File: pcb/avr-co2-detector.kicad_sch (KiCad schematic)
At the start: 7 parts

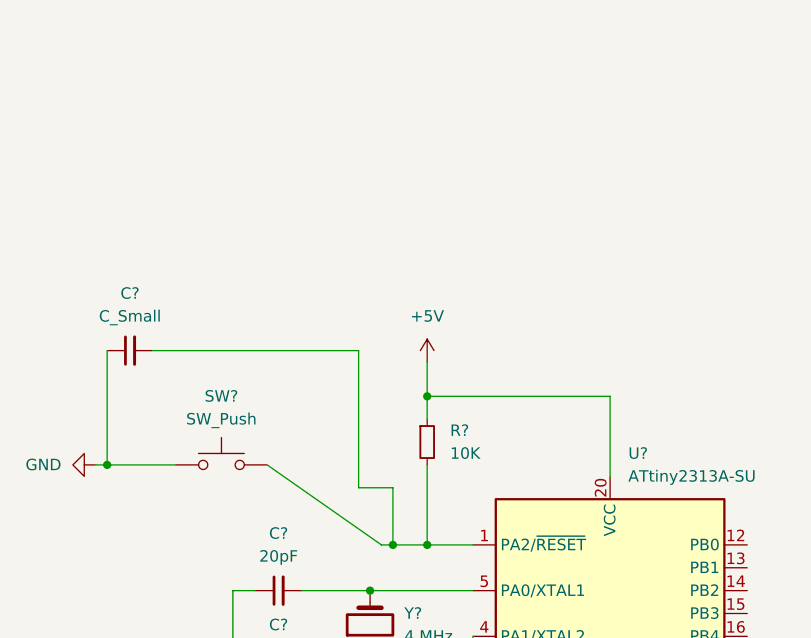
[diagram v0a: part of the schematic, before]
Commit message: Added USB Type-C connector for power supply, decoupling capacitor for ATtiny2313A
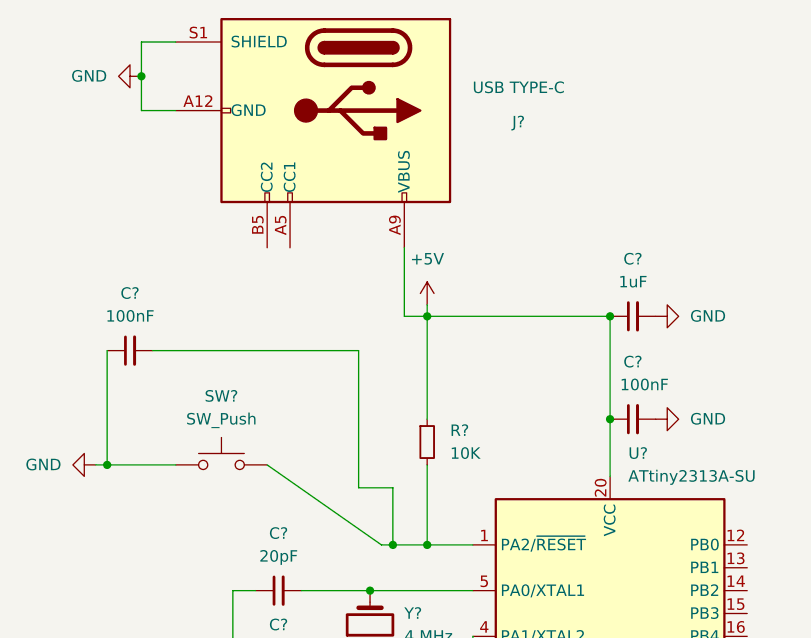
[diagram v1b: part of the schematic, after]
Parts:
- added C?: 1uF, symbol Device:C_Small
- added C?: 100nF, symbol Device:C_Small
- added J?: USB TYPE-C, Connector_USB:USB_C_Receptacle_HRO_TYPE-C-31-M-12, symbol Connector:USB_C_Receptacle_PowerOnly_6P
- C?: value C_Small -> 100nF
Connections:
- net +5V: now also C?.1, C?.1, J?.A9 (VBUS), J?.B9 (VBUS)
- net GND: now also C?.2, C?.2, J?.A12 (GND), J?.B12 (GND), J?.S1 (SHIELD)
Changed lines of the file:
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@@
 (kicad_sch (version 20211123) (generator eeschema)
   (paper "A4")
+  (junction (at 78.74 46.99) (diameter 0) (color 0 0 0 0)
+  )
   (junction (at 88.9 114.3) (diameter 0) (color 0 0 0 0)
   )
@@
   (junction (at 104.14 111.76) (diameter 0) (color 0 0 0 0)
   )
+  (junction (at 130.81 85.09) (diameter 0) (color 0 0 0 0)
+  )
+  (junction (at 110.49 73.66) (diameter 0) (color 0 0 0 0)
+  )
   (junction (at 106.68 99.06) (diameter 0) (color 0 0 0 0)
   )
-  (junction (at 110.49 82.55) (diameter 0) (color 0 0 0 0)
-  )
   (junction (at 110.49 99.06) (diameter 0) (color 0 0 0 0)
   )
   (junction (at 104.14 104.14) (diameter 0) (color 0 0 0 0)
   )
-  (wire (pts (xy 130.81 91.44) (xy 130.81 82.55))
+  (junction (at 130.81 73.66) (diameter 0) (color 0 0 0 0)
+  )
+  (wire (pts (xy 78.74 43.18) (xy 78.74 46.99))
+    (stroke (width 0) (type default) (color 0 0 0 0))
+  )
+  (wire (pts (xy 107.95 66.04) (xy 107.95 73.66))
     (stroke (width 0) (type default) (color 0 0 0 0))
   )
@@
     (stroke (width 0) (type default) (color 0 0 0 0))
   )
+  (wire (pts (xy 82.55 43.18) (xy 78.74 43.18))
+    (stroke (width 0) (type default) (color 0 0 0 0))
+  )
   (wire (pts (xy 104.14 104.14) (xy 115.57 104.14))
     (stroke (width 0) (type default) (color 0 0 0 0))
@@
     (stroke (width 0) (type default) (color 0 0 0 0))
   )
+  (wire (pts (xy 110.49 73.66) (xy 130.81 73.66))
+    (stroke (width 0) (type default) (color 0 0 0 0))
+  )
   (wire (pts (xy 105.41 99.06) (xy 106.68 99.06))
     (stroke (width 0) (type default) (color 0 0 0 0))
   )
+  (wire (pts (xy 82.55 50.8) (xy 78.74 50.8))
+    (stroke (width 0) (type default) (color 0 0 0 0))
+  )
   (wire (pts (xy 88.9 104.14) (xy 88.9 114.3))
     (stroke (width 0) (type default) (color 0 0 0 0))
@@
     (stroke (width 0) (type default) (color 0 0 0 0))
   )
-  (wire (pts (xy 110.49 82.55) (xy 110.49 85.09))
+  (wire (pts (xy 130.81 73.66) (xy 130.81 85.09))
+    (stroke (width 0) (type default) (color 0 0 0 0))
+  )
+  (wire (pts (xy 110.49 73.66) (xy 110.49 85.09))
     (stroke (width 0) (type default) (color 0 0 0 0))
   )
@@
     (stroke (width 0) (type default) (color 0 0 0 0))
   )
+  (wire (pts (xy 130.81 85.09) (xy 130.81 91.44))
+    (stroke (width 0) (type default) (color 0 0 0 0))
+  )
   (wire (pts (xy 115.57 111.76) (xy 115.57 109.22))
     (stroke (width 0) (type default) (color 0 0 0 0))
@@
     (stroke (width 0) (type default) (color 0 0 0 0))
   )
-  (wire (pts (xy 110.49 82.55) (xy 130.81 82.55))
+  (wire (pts (xy 107.95 73.66) (xy 110.49 73.66))
     (stroke (width 0) (type default) (color 0 0 0 0))
   )
@@
     (stroke (width 0) (type default) (color 0 0 0 0))
   )
-  (wire (pts (xy 110.49 78.74) (xy 110.49 82.55))
+  (wire (pts (xy 110.49 72.39) (xy 110.49 73.66))
     (stroke (width 0) (type default) (color 0 0 0 0))
   )
   (wire (pts (xy 102.87 77.47) (xy 102.87 92.71))
+    (stroke (width 0) (type default) (color 0 0 0 0))
+  )
+  (wire (pts (xy 78.74 50.8) (xy 78.74 46.99))
     (stroke (width 0) (type default) (color 0 0 0 0))
   )
@@
     (pin "1")
   )
+  (symbol (lib_id "Device:C_Small") (at 133.35 73.66 90) (unit 1)
+    (in_bom yes) (on_board yes)
+    (property "Reference" "C?" (id 0) (at 133.3563 67.31 90))
+    (property "Value" "1uF" (id 1) (at 133.3563 69.85 90))
+    (property "Footprint" "" (id 2) (at 133.35 73.66 0)
+      (effects (font (size 1.27 1.27)) hide)
+    )
+    (property "Datasheet" "~" (id 3) (at 133.35 73.66 0)
+      (effects (font (size 1.27 1.27)) hide)
+    )
+    (pin "1")
+    (pin "2")
+  )
+  (symbol (lib_id "power:GND") (at 135.89 85.09 90) (unit 1)
+    (in_bom yes) (on_board yes) (fields_autoplaced)
+    (property "Reference" "#PWR?" (id 0) (at 142.24 85.09 0)
+      (effects (font (size 1.27 1.27)) hide)
+    )
+    (property "Value" "GND" (id 1) (at 139.7 85.0899 90)
+      (effects (font (size 1.27 1.27)) (justify right))
+    )
+    (property "Footprint" "" (id 2) (at 135.89 85.09 0)
+      (effects (font (size 1.27 1.27)) hide)
+    )
+    (property "Datasheet" "" (id 3) (at 135.89 85.09 0)
+      (effects (font (size 1.27 1.27)) hide)
+    )
+    (pin "1")
+  )
   (symbol (lib_id "Device:R_Small") (at 110.49 87.63 0) (unit 1)
     (in_bom yes) (on_board yes) (fields_autoplaced)
@@
     (pin "1")
     (pin "2")
+  )
+  (symbol (lib_id "power:GND") (at 78.74 46.99 270) (unit 1)
+    (in_bom yes) (on_board yes) (fields_autoplaced)
+    (property "Reference" "#PWR?" (id 0) (at 72.39 46.99 0)
+      (effects (font (size 1.27 1.27)) hide)
+    )
+    (property "Value" "GND" (id 1) (at 74.93 46.9899 90)
+      (effects (font (size 1.27 1.27)) (justify right))
+    )
+    (property "Footprint" "" (id 2) (at 78.74 46.99 0)
+      (effects (font (size 1.27 1.27)) hide)
+    )
+    (property "Datasheet" "" (id 3) (at 78.74 46.99 0)
+      (effects (font (size 1.27 1.27)) hide)
+    )
+    (pin "1")
   )
   (symbol (lib_id "MCU_Microchip_ATtiny:ATtiny2313A-S") (at 130.81 119.38 0) (unit 1)
@@
     (pin "2")
   )
+  (symbol (lib_id "Connector:USB_C_Receptacle_PowerOnly_6P") (at 100.33 50.8 270) (unit 1)
+    (in_bom yes) (on_board yes)
+    (property "Reference" "J?" (id 0) (at 120.65 52.07 90))
+    (property "Value" "USB TYPE-C" (id 1) (at 120.65 48.26 90))
+    (property "Footprint" "Connector_USB:USB_C_Receptacle_HRO_TYPE-C-31-M-12" (id 2) (at 102.87 54.61 0)
+      (effects (font (size 1.27 1.27)) hide)
+    )
+    (property "Datasheet" "https://www.usb.org/sites/default/files/documents/usb_type-c.zip" (id 3) (at 100.33 50.8 0)
+      (effects (font (size 1.27 1.27)) hide)
+    )
+    (pin "A12")
+    (pin "A5")
+    (pin "A9")
+    (pin "B12")
+    (pin "B5")
+    (pin "B9")
+    (pin "S1")
+  )
   (symbol (lib_id "power:GND") (at 73.66 90.17 270) (unit 1)
     (in_bom yes) (on_board yes) (fields_autoplaced)
@@
     (in_bom yes) (on_board yes) (fields_autoplaced)
     (property "Reference" "C?" (id 0) (at 77.4763 71.12 90))
-    (property "Value" "C_Small" (id 1) (at 77.4763 73.66 90))
+    (property "Value" "100nF" (id 1) (at 77.4763 73.66 90))
     (property "Footprint" "" (id 2) (at 77.47 77.47 0)
       (effects (font (size 1.27 1.27)) hide)
@@
     (pin "2")
   )
-  (symbol (lib_id "power:+5V") (at 110.49 78.74 0) (unit 1)
-    (in_bom yes) (on_board yes) (fields_autoplaced)
-    (property "Reference" "#PWR?" (id 0) (at 110.49 82.55 0)
-      (effects (font (size 1.27 1.27)) hide)
-    )
-    (property "Value" "+5V" (id 1) (at 110.49 73.66 0))
-    (property "Footprint" "" (id 2) (at 110.49 78.74 0)
-      (effects (font (size 1.27 1.27)) hide)
-    )
-    (property "Datasheet" "" (id 3) (at 110.49 78.74 0)
-      (effects (font (size 1.27 1.27)) hide)
-    )
-    (pin "1")
+  (symbol (lib_id "power:+5V") (at 110.49 72.39 0) (unit 1)
+    (in_bom yes) (on_board yes) (fields_autoplaced)
+    (property "Reference" "#PWR?" (id 0) (at 110.49 76.2 0)
+      (effects (font (size 1.27 1.27)) hide)
+    )
+    (property "Value" "+5V" (id 1) (at 110.49 67.31 0))
+    (property "Footprint" "" (id 2) (at 110.49 72.39 0)
+      (effects (font (size 1.27 1.27)) hide)
+    )
+    (property "Datasheet" "" (id 3) (at 110.49 72.39 0)
+      (effects (font (size 1.27 1.27)) hide)
+    )
+    (pin "1")
+  )
+  (symbol (lib_id "power:GND") (at 135.89 73.66 90) (unit 1)
+    (in_bom yes) (on_board yes) (fields_autoplaced)
+    (property "Reference" "#PWR?" (id 0) (at 142.24 73.66 0)
+      (effects (font (size 1.27 1.27)) hide)
+    )
+    (property "Value" "GND" (id 1) (at 139.7 73.6599 90)
+      (effects (font (size 1.27 1.27)) (justify right))
+    )
+    (property "Footprint" "" (id 2) (at 135.89 73.66 0)
+      (effects (font (size 1.27 1.27)) hide)
+    )
+    (property "Datasheet" "" (id 3) (at 135.89 73.66 0)
+      (effects (font (size 1.27 1.27)) hide)
+    )
+    (pin "1")
+  )
+  (symbol (lib_id "Device:C_Small") (at 133.35 85.09 90) (unit 1)
+    (in_bom yes) (on_board yes)
+    (property "Reference" "C?" (id 0) (at 133.3563 78.74 90))
+    (property "Value" "100nF" (id 1) (at 134.62 81.28 90))
+    (property "Footprint" "" (id 2) (at 133.35 85.09 0)
+      (effects (font (size 1.27 1.27)) hide)
+    )
+    (property "Datasheet" "~" (id 3) (at 133.35 85.09 0)
+      (effects (font (size 1.27 1.27)) hide)
+    )
+    (pin "1")
+    (pin "2")
   )
   (symbol (lib_id "Device:C_Small") (at 93.98 104.14 90) (unit 1)
@@
       (reference "#PWR?") (unit 1) (value "GND") (footprint "")
     )
+    (path "/2105c66b-291c-4c0c-8c48-8cbbc6af028c"
+      (reference "#PWR?") (unit 1) (value "GND") (footprint "")
+    )
+    (path "/41182ee8-78dc-45c9-8616-06bc53e6952c"
+      (reference "#PWR?") (unit 1) (value "GND") (footprint "")
+    )
     (path "/681e6531-f03d-4de8-84f7-af0a14c68e8e"
       (reference "#PWR?") (unit 1) (value "GND") (footprint "")
@@
       (reference "#PWR?") (unit 1) (value "+5V") (footprint "")
     )
+    (path "/c5db6a54-9818-4823-8978-b12ba5ae3bf3"
+      (reference "#PWR?") (unit 1) (value "GND") (footprint "")
+    )
     (path "/fb7a8f19-66da-46d2-94ca-ca9fbfb4de4b"
       (reference "#PWR?") (unit 1) (value "GND") (footprint "")
     )
+    (path "/1e1df36f-397a-4f2b-b60d-e2448815c475"
+      (reference "C?") (unit 1) (value "1uF") (footprint "")
+    )
     (path "/9027a3cb-d61e-47fa-a79d-fba2d8e0022e"
-      (reference "C?") (unit 1) (value "C_Small") (footprint "")
+      (reference "C?") (unit 1) (value "100nF") (footprint "")
+    )
+    (path "/c83c64e5-cb8b-4db2-832b-a15f648124fc"
+      (reference "C?") (unit 1) (value "100nF") (footprint "")
     )
     (path "/dab70801-e4c5-4fe2-88e9-e170ed9e81ee"
@@
       (reference "C?") (unit 1) (value "20pF") (footprint "")
     )
+    (path "/56963627-a9df-4434-983c-b60a2bd5363c"
+      (reference "J?") (unit 1) (value "USB TYPE-C") (footprint "Connector_USB:USB_C_Receptacle_HRO_TYPE-C-31-M-12")
+    )
     (path "/280b1d14-beed-40a9-b10e-e8b499e88613"

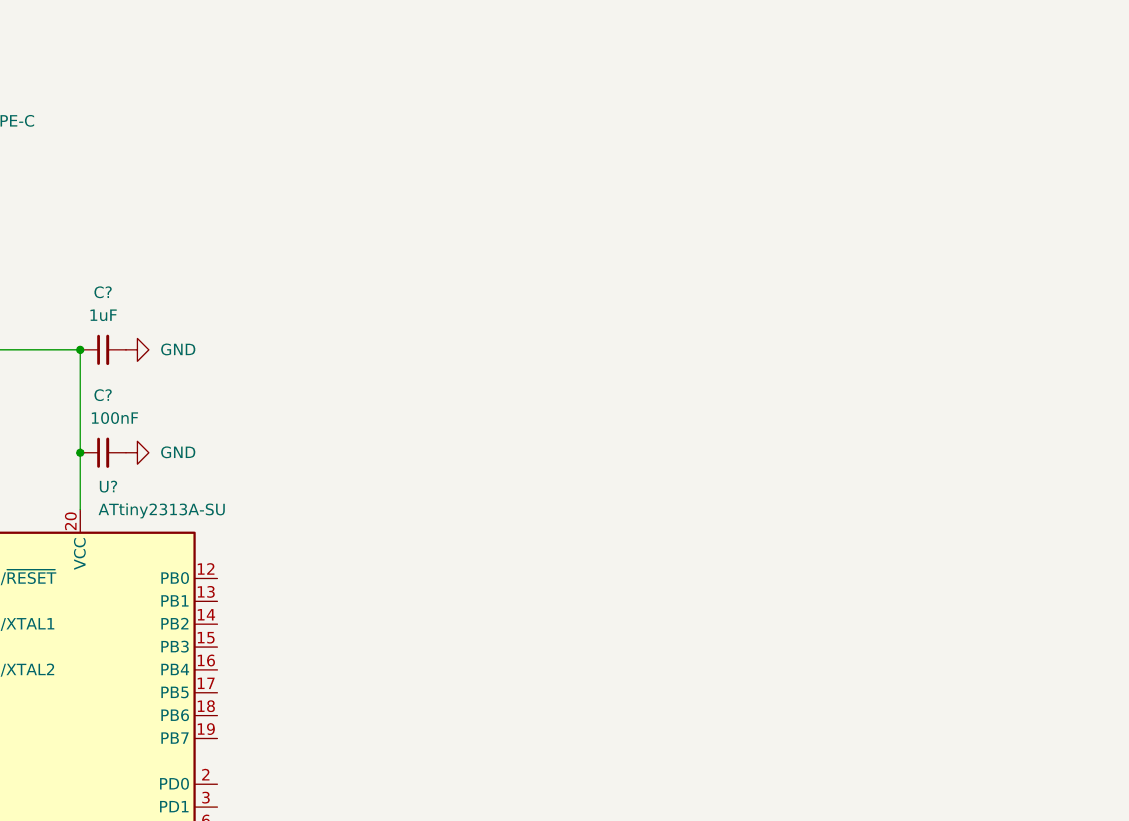
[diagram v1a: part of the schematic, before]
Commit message: Added voltage regulator (3.3V) and ESP-07 module
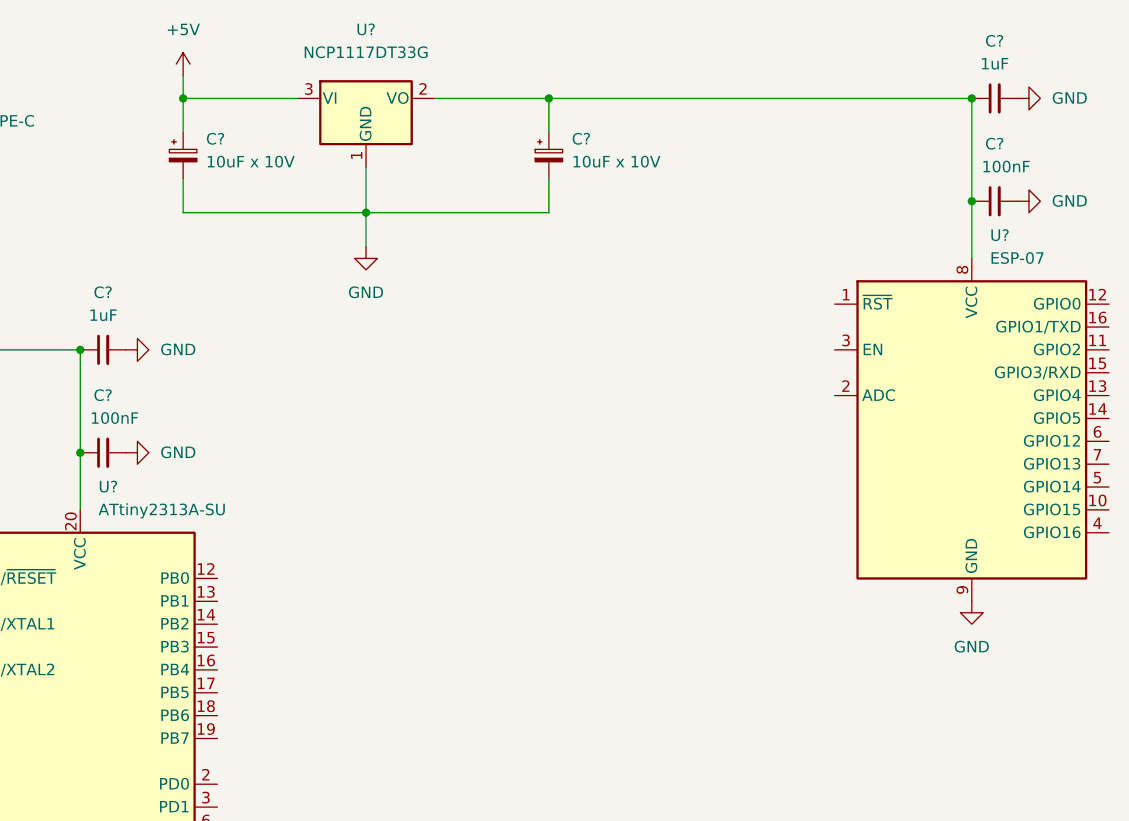
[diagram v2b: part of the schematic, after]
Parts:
- added C? (x2): 10uF x 10V, symbol Device:C_Polarized_Small
- added C?: 1uF, symbol Device:C_Small
- added C?: 100nF, symbol Device:C_Small
- added U?: ESP-07, RF_Module:ESP-07, symbol RF_Module:ESP-07
- added U?: NCP1117DT33G, Package_TO_SOT_SMD:TO-252-2, symbol Regulator_Linear:NCP1117-3.3_TO252
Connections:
- net +5V: now also C?.1, U?.3 (VI)
- net GND: now also C?.2, C?.2, C?.2, C?.2, U?.1 (GND), U?.9 (GND)
- new net: C?.1, C?.1, C?.1, U?.2 (VO), U?.8 (VCC)
